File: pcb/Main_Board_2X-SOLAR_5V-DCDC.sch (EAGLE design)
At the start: 66 parts, among them CN5 USBA_FEMALE, M3AB FDMC8030, M4 SI7611DN, M5 FDMC8327L, T2 MMUN2133LT1G, U1 LTC4015EUHFPBFQFN-38_UHF-M, U3 TPS61090RSAR, X1 6V_PV

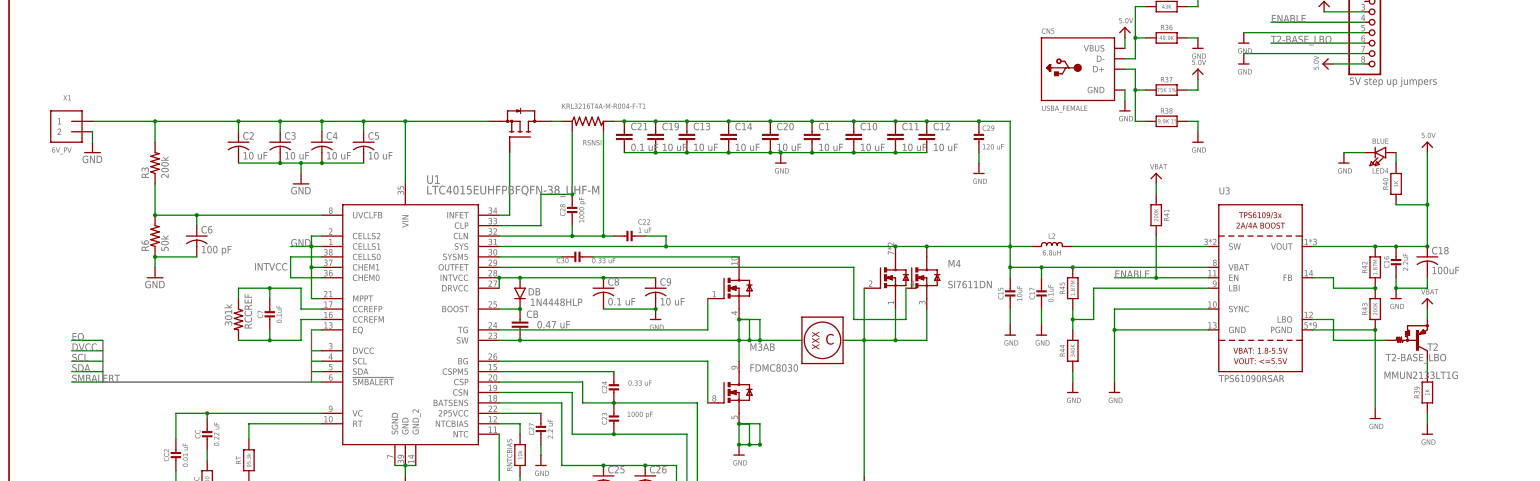
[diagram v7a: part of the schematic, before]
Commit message: Board layout finished
PCB board layout finished. Final errors to review are related to package pad clearances.
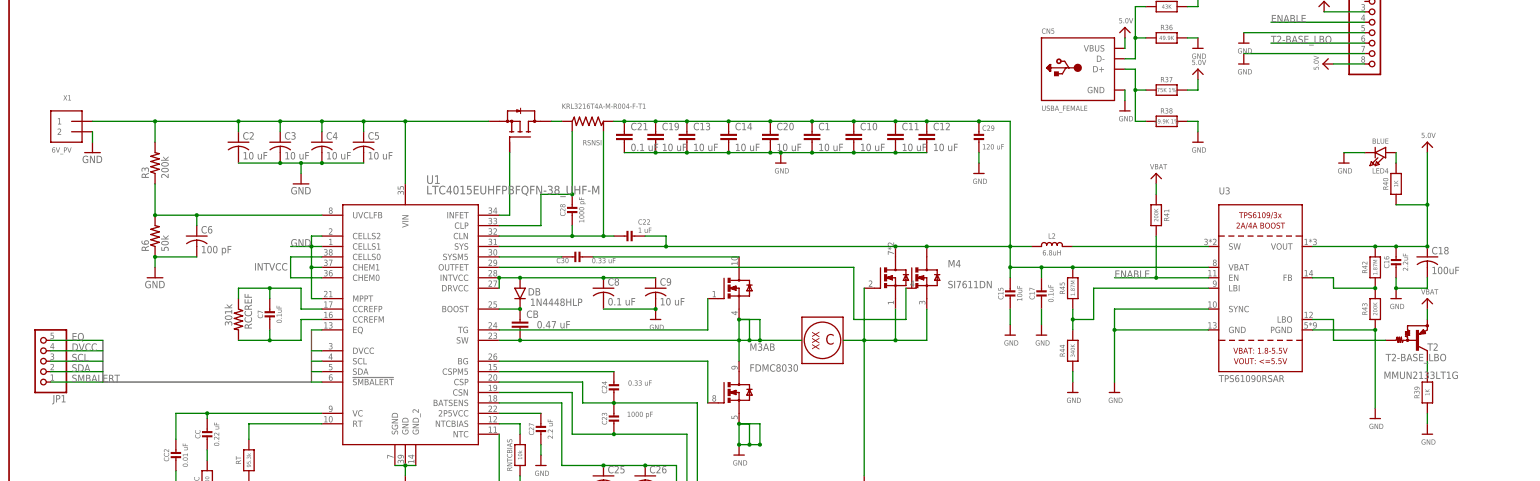
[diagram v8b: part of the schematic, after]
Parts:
- added JP1: (no value), pinhead:PINHD-1X5
- JP10: value 5V step up jumpers -> (none)
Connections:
- net N$1 renamed OUTFET_M4_SOURCE
- net DVCC: now also JP1.4
- net EQ: now also JP1.5
- net SCL: now also JP1.3
- net SDA: now also JP1.2
- net SMBALERT: now also JP1.1
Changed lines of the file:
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@@
 <layer number="17" name="Pads" color="2" fill="1" visible="no" active="no"/>
 <layer number="18" name="Vias" color="2" fill="1" visible="no" active="no"/>
-<layer number="19" name="Unrouted" color="6" fill="1" visible="no" active="no"/>
+<layer number="19" name="Unrouted" color="61" fill="1" visible="no" active="no"/>
 <layer number="20" name="Dimension" color="15" fill="1" visible="no" active="no"/>
 <layer number="21" name="tPlace" color="7" fill="1" visible="no" active="no"/>
@@
 <part name="C18" library="rcl" deviceset="C-US" device="C1210" value="100uF"/>
 <part name="U$81" library="microbuilder" deviceset="GND" device=""/>
-<part name="JP10" library="microbuilder" deviceset="HEADER-1X8" device="ROUND" value="5V step up jumpers"/>
+<part name="JP10" library="microbuilder" deviceset="HEADER-1X8" device="ROUND"/>
 <part name="U$82" library="microbuilder" deviceset="VBUS" device=""/>
 <part name="U1" library="LTC4015_LTC4015EUHF&amp;hash_PBF" deviceset="LTC4015EUHFPBF" device="QFN-38_UHF-M"/>
@@
 <part name="U$14" library="microbuilder" deviceset="GND" device=""/>
 <part name="C30" library="microbuilder" deviceset="CAP_CERAMIC" device="0805-NOOUTLINE" value="0.33 uF"/>
+<part name="JP1" library="pinhead" library_urn="urn:adsk.eagle:library:325" deviceset="PINHD-1X5" device=""/>
 </parts>
 <sheets>
@@
 <attribute name="VALUE" x="147.808" y="119.112" size="1.27" layer="96" font="vector" align="top-right"/>
 </instance>
+<instance part="JP1" gate="A" x="7.62" y="93.98" rot="R180"/>
 </instances>
 <busses>
@@
 <pinref part="U1" gate="A" pin="INTVCC"/>
 <wire x1="119.38" y1="111.76" x2="119.38" y2="114.3" width="0.1524" layer="91"/>
-<wire x1="119.38" y1="114.3" x2="124.46" y2="114.3" width="0.1524" layer="91"/>
 <junction x="119.38" y="114.3"/>
 <pinref part="C9" gate="G$1" pin="1"/>
@@
 <pinref part="DB" gate="G$1" pin="P$2"/>
 <junction x="124.46" y="114.3"/>
+<wire x1="119.38" y1="114.3" x2="124.46" y2="114.3" width="0.1524" layer="91"/>
 </segment>
 <segment>
@@
 </segment>
 <segment>
-<wire x1="15.24" y1="93.98" x2="22.86" y2="93.98" width="0.1524" layer="91"/>
+<wire x1="10.16" y1="93.98" x2="22.86" y2="93.98" width="0.1524" layer="91"/>
 <label x="15.24" y="93.98" size="1.778" layer="95"/>
+<pinref part="JP1" gate="A" pin="3"/>
 </segment>
 </net>
@@
 </segment>
 <segment>
-<wire x1="15.24" y1="91.44" x2="22.86" y2="91.44" width="0.1524" layer="91"/>
+<wire x1="10.16" y1="91.44" x2="22.86" y2="91.44" width="0.1524" layer="91"/>
 <label x="15.24" y="91.44" size="1.778" layer="95"/>
+<pinref part="JP1" gate="A" pin="2"/>
 </segment>
 </net>
@@
 </segment>
 <segment>
-<wire x1="15.24" y1="88.9" x2="22.86" y2="88.9" width="0.1524" layer="91"/>
+<wire x1="10.16" y1="88.9" x2="22.86" y2="88.9" width="0.1524" layer="91"/>
 <label x="15.24" y="88.9" size="1.778" layer="95"/>
+<pinref part="JP1" gate="A" pin="1"/>
 </segment>
 </net>
@@
 </segment>
 <segment>
-<wire x1="22.86" y1="96.52" x2="15.24" y2="96.52" width="0.1524" layer="91"/>
+<wire x1="22.86" y1="96.52" x2="10.16" y2="96.52" width="0.1524" layer="91"/>
 <label x="15.24" y="96.52" size="1.778" layer="95"/>
+<pinref part="JP1" gate="A" pin="4"/>
 </segment>
 </net>
@@
 </segment>
 <segment>
-<wire x1="22.86" y1="99.06" x2="15.24" y2="99.06" width="0.1524" layer="91"/>
+<wire x1="22.86" y1="99.06" x2="10.16" y2="99.06" width="0.1524" layer="91"/>
 <label x="15.24" y="99.06" size="1.778" layer="95"/>
-</segment>
-</net>
-<net name="N$1" class="0">
+<pinref part="JP1" gate="A" pin="5"/>
+</segment>
+</net>
+<net name="OUTFET_M4_SOURCE" class="0">
 <segment>
 <pinref part="M4" gate="G$1" pin="S1"/>
